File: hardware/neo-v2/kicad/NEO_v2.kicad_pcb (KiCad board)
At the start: 4 copper layers, 84 x 89 mm, 498 parts, among them J1 ST-PJ-930A, J2 WY-3315, J201 OLED I2C, Q1 CJ3407, Q10 LBSS138WT1G, Q2 LBSS138WT1G, Q201 FS8205A, Q202 FS8205A, Q203 CSD25402Q3A, Q3 LBSS138WT1G, Q4 S9013W, Q6 LBSS138WT1G, SW1 SK-22H07, SW2 AN-P1S-2SP-Z, SW201 MSK-22D18G3, SW3 MK-12C02 G1.5, U1 ESP32-S3R8, U10 TPS62827DMQR, U11 ME6211C18M5G-N, U12 TPS62065DSGR, U14 SN74LVC1G17DCKR, U15 ZB25VQ128DSJG, U16 W25Q256JVEIQ, U17 SGM7222YWQ10/TR, U18 SGM2036S-3.3XXDH4G/TR, U19 LC1458CB5TR33, U2 XU316-1024-QF60B-C24​, U201 TPS2121RUXR, U202 TPS61022RWUT, U203 BQ25170DSGR, U204 MAX17048G+T10, U205 DW01A, U206 LM66200DRLR, U3 ZB25VQ32DSJG, U4 MSM261DHP006, U5 MSM261DHP006, U6 SN74LVC125APWR, U7 SN74LVC1G17DCKR, U8 TLV320AIC3204IRHBR, U9 TPA6211A1DGNR, X1 24MHz 12pF, X2 40MHz

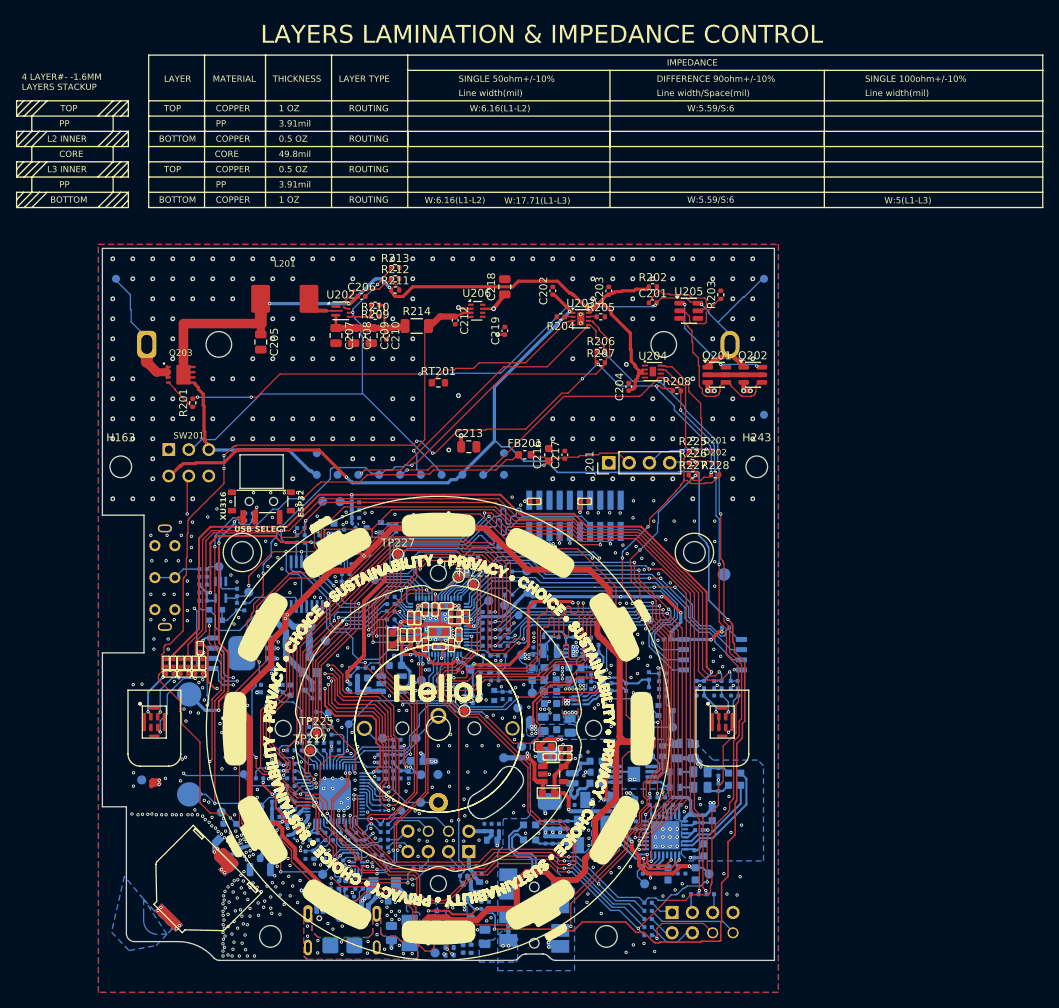
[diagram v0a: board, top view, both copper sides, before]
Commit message: NEO v2 fase 6: paquete de fabricación para JLCPCB
- production/: Gerber de 4 capas y taladros Excellon (PTH/NPTH separados) en zip,
  BOM y CPL en formato JLCPCB (tools/fab_outputs.py).
- Disponibilidad en JLCPCB de las 369 piezas (tools/jlc_bom.py): 15 heredadas
  sustituidas solo en la BOM (tabla SUBST, con estado de verificación de huella),
  3 cambios de código por stock y 5 piezas consignadas (ANT2, J1, SW1, SW2, USB1).
  Las hojas de Nabu Casa no cambian.
- Huellas: WS2812B-2020-V6 y cristal JLYE de 40 MHz verificados contra plano;
  U206 LM66200 añadida a la tabla de verificación (TI DRL0008A).
- Serigrafía (tools/silk_cleanup.py, integrado en build_pcb.sh): referencias de lo
  nuevo a Fab como en el original, etiquetas de TP/conectores sin solapes, tabla de
  apilado exterior a Cmts.User y aviso de origen y licencia en la cara B.
- Tabla de rotaciones KiCad/EasyEDA para revisar en la vista previa de JLCPCB.
- erc_annotations.py: referencias #FLG95xx (evita el aviso de anotación duplicada).
- docs/fase6-fabricacion.md: lista de revisión previa al pedido y riesgos
  residuales ordenados por gravedad. CHANGES y README actualizados.

Reconstrucción completa: DRC con paridad 0/0/0 (15 exclusiones heredadas
comentadas), ERC 0 errores, verify_netlist OK.

Co-Authored-By: Claude Opus 5.5 <noreply@anthropic.com>
Claude-Session: https://claude.ai/code/session_01UWwWJAyCeb1aBHbGbkDaMx
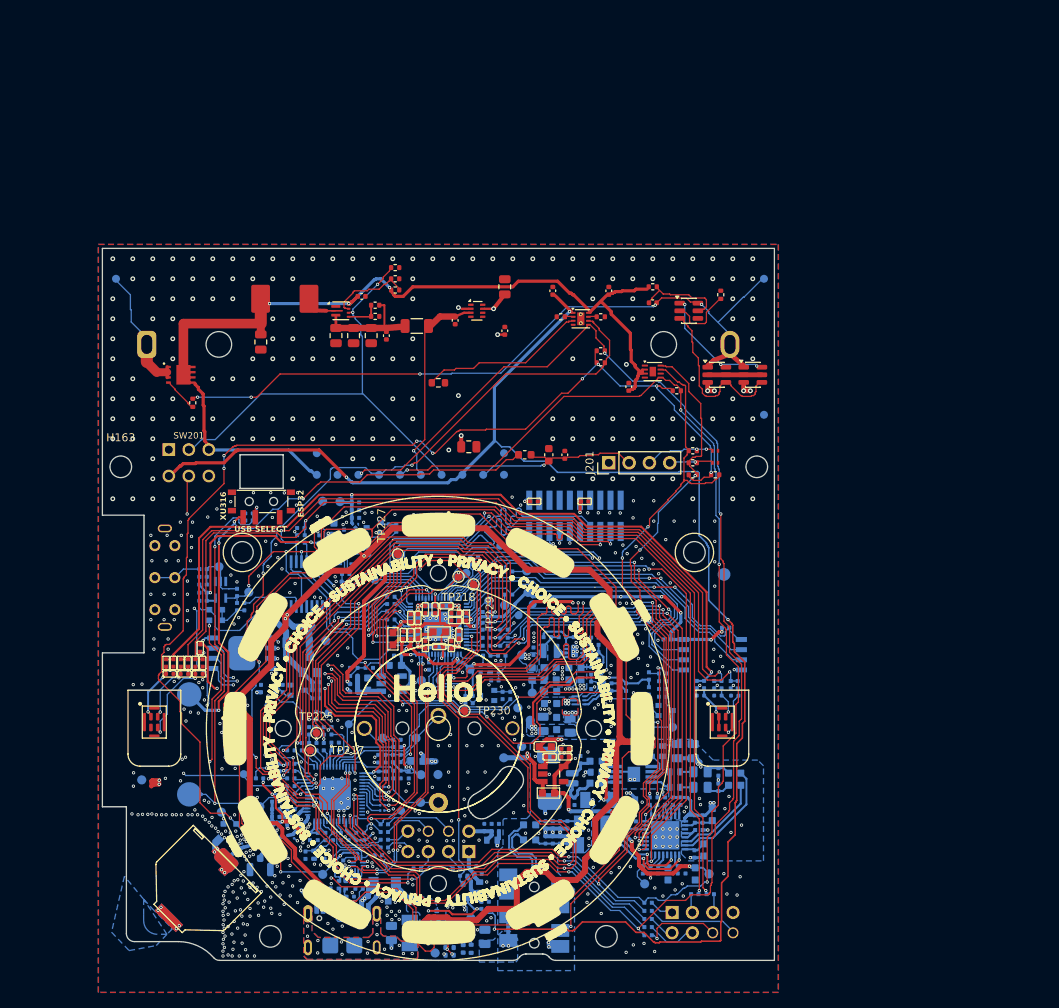
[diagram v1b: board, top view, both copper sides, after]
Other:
- board text added: "CERN-OHL-P v2 - bloques nuevos: techmiguel"
- board text added: "NEO v2 - derivado de Home Assistant Voice PE (Nabu Casa)"
